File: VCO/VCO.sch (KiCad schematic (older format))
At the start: 22 parts, among them J1 JACK_STEREO, Q1 Q_NMOS_SGD, SW1 SWITCH_INV, U1 LM324

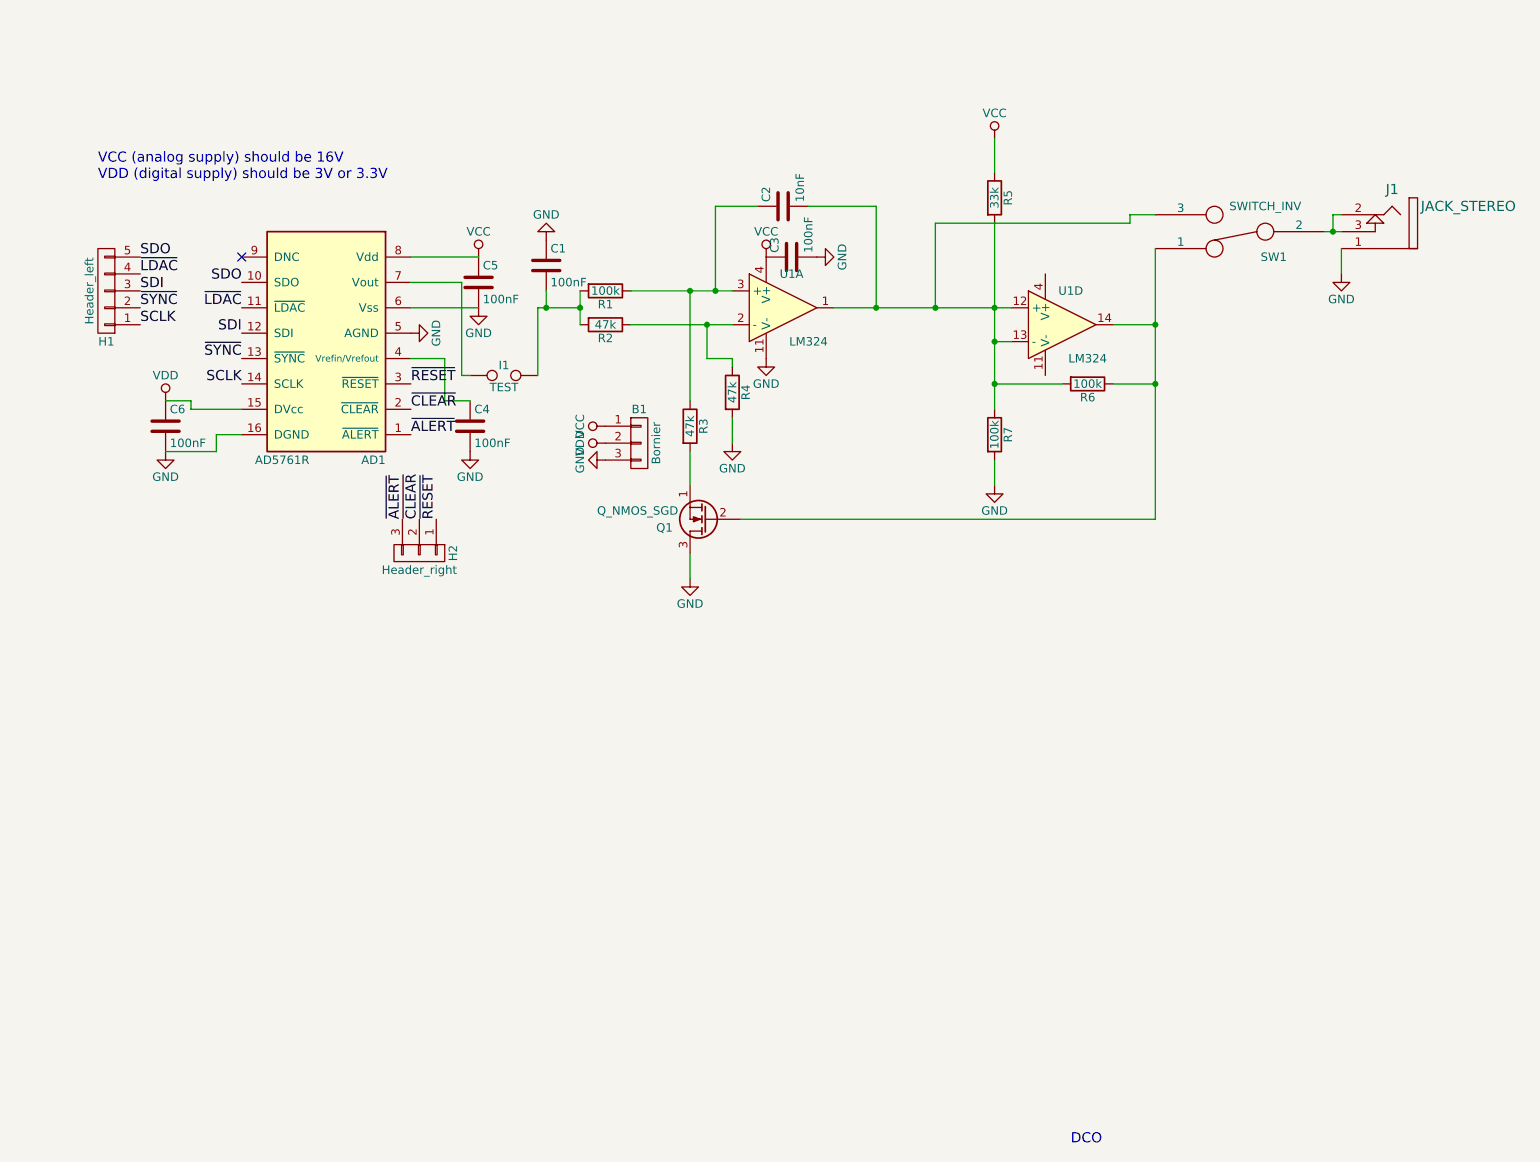
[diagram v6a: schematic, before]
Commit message: Fixed VCO
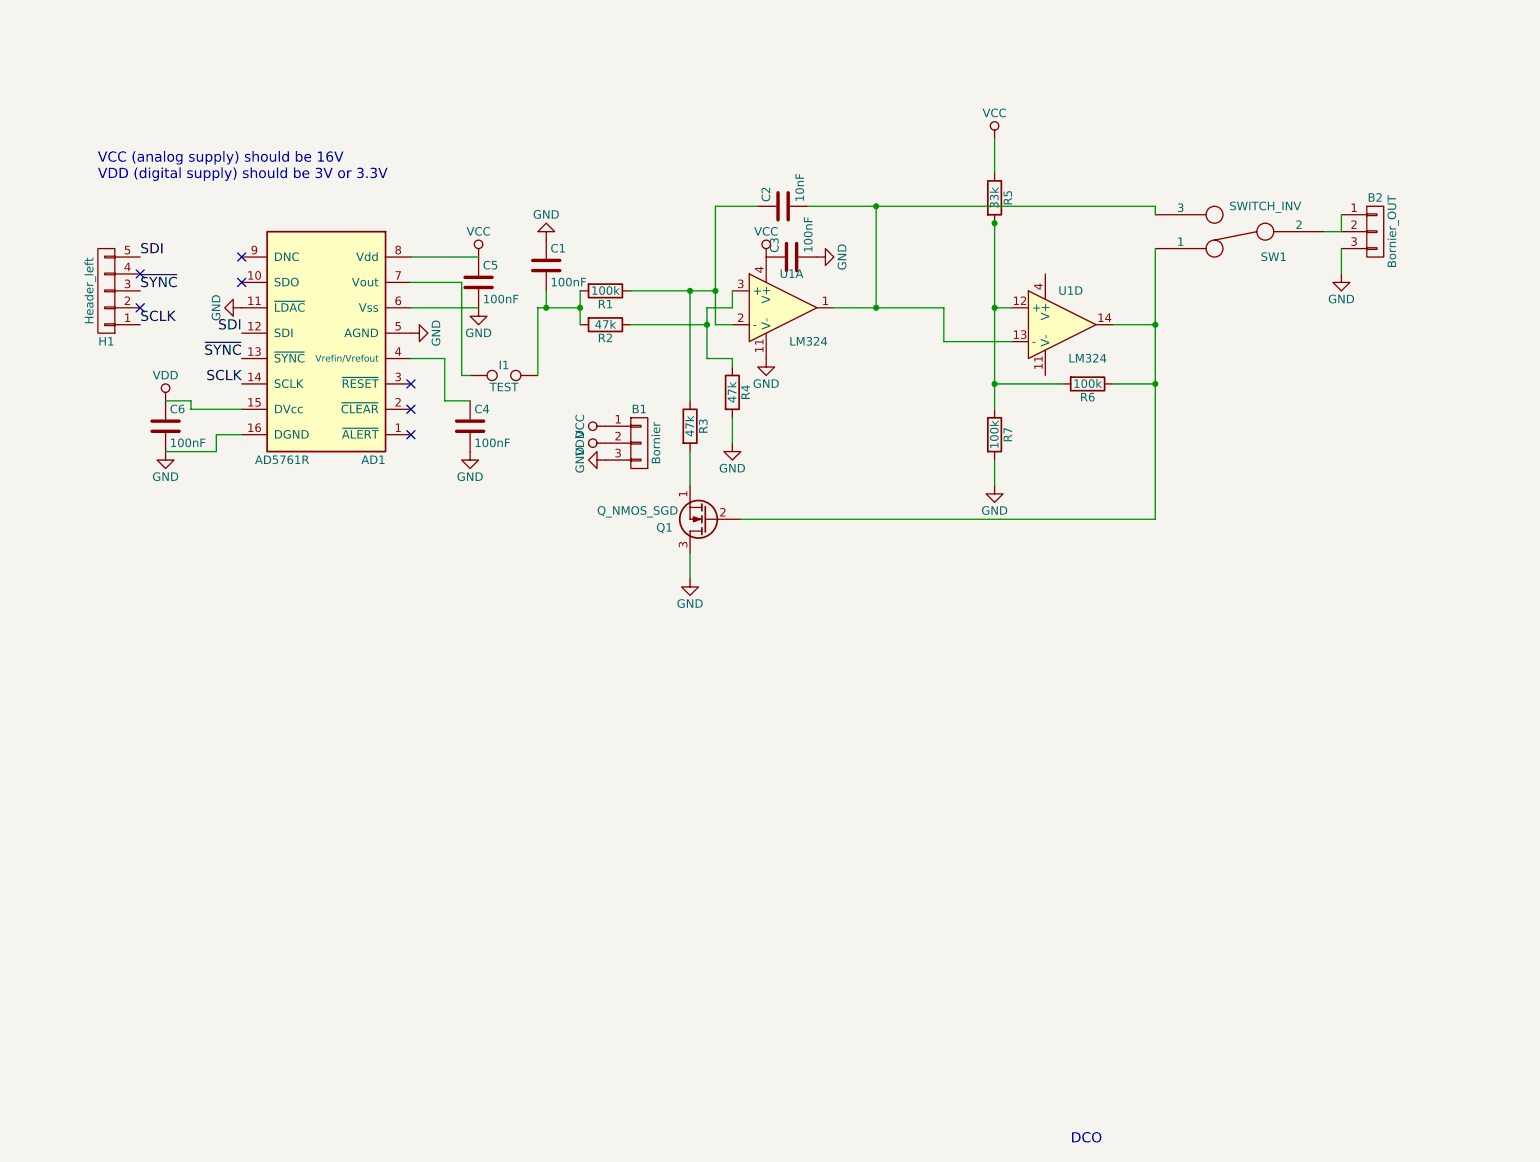
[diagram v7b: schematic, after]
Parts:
- removed H2: Header_right, Pin_Headers:Pin_Header_Straight_1x03_Pitch2.54mm, symbol CONN_01X03
- removed J1: JACK_STEREO, jack:jack-stereo, symbol JACK_MONO
- added B2: Bornier_OUT, bornier:Bornier_3pins, symbol CONN_01X03
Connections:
- net GND: now also AD1.11 (~LDAC), B2.3 (P3)
- net SDI: now also H1.5 (P5); no longer H1.3 (P3)
- net ~SYNC: now also H1.3 (P3); no longer H1.2 (P2)
- net at C2.1, R1.1, R3.1: now also U1.2 (-); no longer U1.3 (+)
- net at C2.2, SW1.3, U1.1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: no longer R5.2, R6.2, R7.1, U1.12 (+)
- net at R2.1, R4.1: now also U1.3 (+); no longer U1.2 (-)
- net at SW1.2: now also B2.1 (P1), B2.2 (P2)
- net SDO: no longer names the net of AD1.10 (SDO)
- net SDO: no longer H1.5 (P5)
- net ~ALERT: no longer names the net of AD1.1 (~ALERT)
- net ~CLEAR: no longer names the net of AD1.2 (~CLEAR)
- net ~LDAC: no longer names the net of H1.4 (P4)
- net ~LDAC: no longer AD1.11 (~LDAC)
- net ~RESET: no longer names the net of AD1.3 (~RESET)
- new net: R5.2, R6.2, R7.1, U1.12 (+)
- no-connect marks 1 -> 7
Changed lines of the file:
@@
-$EndComp
-$Comp
-L JACK_MONO J1
-U 1 1 58D1CA56
-P 9300 2100
-F 0 "J1" H 9300 2350 60  0000 C CNN
-F 1 "JACK_STEREO" H 9750 2250 60  0000 C CNN
-F 2 "jack:jack-stereo" H 9550 2150 60  0001 C CNN
-F 3 "" H 9550 2150 60  0000 C CNN
-	1    9300 2100
-	1    0    0    -1
 $EndComp
 $Comp
@@
 $EndComp
 NoConn ~ 2500 2250
-Text Label 2500 2400 2    60   ~ 0
-SDO
-Text Label 1900 2250 0    60   ~ 0
-SDO
-Text Label 2500 2550 2    60   ~ 0
-~LDAC
-Text Label 1900 2350 0    60   ~ 0
-~LDAC
 $Comp
 L C C6
@@
 Text Label 2500 2850 2    60   ~ 0
 ~SYNC
-Text Label 1900 2550 0    60   ~ 0
+Text Label 1900 2450 0    60   ~ 0
 ~SYNC
 Text Label 2500 3000 2    60   ~ 0
@@
 Text Label 1900 2650 0    60   ~ 0
 SCLK
-Text Label 3500 3000 0    60   ~ 0
-~RESET
-Text Label 3650 3800 1    60   ~ 0
-~RESET
-Text Label 3500 3150 0    60   ~ 0
-~CLEAR
-Text Label 3550 3800 1    60   ~ 0
-~CLEAR
-Text Label 3500 3300 0    60   ~ 0
-~ALERT
-Text Label 3450 3800 1    60   ~ 0
-~ALERT
 $Comp
 L C C5
@@
 Text Label 2500 2700 2    60   ~ 0
 SDI
-Text Label 1900 2450 0    60   ~ 0
+Text Label 1900 2250 0    60   ~ 0
 SDI
 $Comp
@@
 	-1   0    0    1
 $EndComp
-Wire Wire Line
-	4800 2650 5400 2650
-Wire Wire Line
-	4800 2450 5400 2450
-Wire Wire Line
-	5150 2450 5150 3100
-Connection ~ 5150 2450
-Wire Wire Line
-	5150 3400 5150 3600
-Wire Wire Line
-	5150 4000 5150 4150
-Wire Wire Line
-	5250 2650 5250 2850
-Wire Wire Line
-	5250 2850 5400 2850
-Wire Wire Line
-	5400 2850 5400 2900
-Connection ~ 5250 2650
-Wire Wire Line
-	5400 3200 5400 3350
-Wire Wire Line
-	5300 2450 5300 1950
-Wire Wire Line
-	5300 1950 5550 1950
-Connection ~ 5300 2450
-Connection ~ 6250 2550
-Wire Wire Line
-	6950 3000 7350 3000
-Wire Wire Line
-	6950 2050 6950 3150
-Connection ~ 6950 2550
-Wire Wire Line
-	6950 2750 7050 2750
-Connection ~ 6950 2750
-Wire Wire Line
-	6950 1550 6950 1750
-Connection ~ 6950 3000
-Wire Wire Line
-	6950 3450 6950 3600
-Wire Wire Line
-	7900 3800 5450 3800
-Wire Wire Line
-	7900 2200 7900 3800
-Wire Wire Line
-	7650 3000 7900 3000
-Connection ~ 7900 3000
-Connection ~ 4500 2550
-Wire Wire Line
-	4300 2450 4300 2550
-Connection ~ 4300 2550
-Wire Wire Line
-	6600 2050 6600 2550
-Connection ~ 6600 2550
-Connection ~ 7900 2650
-Wire Wire Line
-	6250 1950 6250 2550
-Wire Wire Line
-	6000 2550 7050 2550
-Wire Wire Line
-	4500 2550 4250 2550
-Wire Wire Line
-	4250 2550 4250 2950
-Wire Wire Line
-	3500 2400 3800 2400
-Wire Wire Line
-	3800 2400 3800 2950
-Wire Wire Line
-	3800 2950 3850 2950
-Wire Wire Line
-	3500 2850 3700 2850
-Wire Wire Line
-	3700 2850 3700 3100
-Wire Wire Line
-	4500 2450 4500 2650
-Wire Wire Line
-	3500 2250 3900 2250
-Wire Wire Line
-	3700 3100 3850 3100
-Wire Wire Line
-	6250 1950 5850 1950
-Wire Wire Line
-	2500 3300 2350 3300
-Wire Wire Line
-	2350 3300 2350 3400
-Wire Wire Line
-	2350 3400 2050 3400
-Wire Wire Line
-	2500 3150 2200 3150
-Wire Wire Line
-	2200 3150 2200 3100
-Wire Wire Line
-	3500 2550 3900 2550
-Wire Wire Line
-	2200 3100 2050 3100
-Wire Wire Line
-	7650 2650 7900 2650
-Wire Wire Line
-	6600 2050 7750 2050
-Wire Wire Line
-	7750 2050 7750 2000
-Wire Wire Line
-	7750 2000 7900 2000
-Wire Wire Line
-	8900 2100 9000 2100
-Wire Wire Line
-	8950 2100 8950 2000
-Wire Wire Line
-	8950 2000 9000 2000
-Connection ~ 8950 2100
-Wire Wire Line
-	9000 2350 9000 2200
 $Comp
 L CONN_01X05 H1
@@
 	-1   0    0    1
 $EndComp
-$Comp
-L CONN_01X03 H2
-U 1 1 58EFE144
-P 3550 4000
-F 0 "H2" H 3550 4200 50  0000 C CNN
-F 1 "Header_right" V 3650 4000 50  0000 C CNN
-F 2 "Pin_Headers:Pin_Header_Straight_1x03_Pitch2.54mm" H 3550 4000 50  0001 C CNN
-F 3 "" H 3550 4000 50  0000 C CNN
-	1    3550 4000
+Wire Wire Line
+	5150 3400 5150 3600
+Wire Wire Line
+	5150 4000 5150 4150
+Wire Wire Line
+	5250 2550 5250 2850
+Wire Wire Line
+	5250 2850 5400 2850
+Wire Wire Line
+	5400 2850 5400 2900
+Connection ~ 5250 2650
+Wire Wire Line
+	5400 3200 5400 3350
+Wire Wire Line
+	5300 1950 5300 2650
+Wire Wire Line
+	5300 1950 5550 1950
+Connection ~ 5300 2450
+Connection ~ 6250 2550
+Wire Wire Line
+	6650 2750 7050 2750
+Wire Wire Line
+	6950 1550 6950 1750
+Wire Wire Line
+	6950 3450 6950 3600
+Wire Wire Line
+	7900 3800 5450 3800
+Wire Wire Line
+	7900 2200 7900 3800
+Wire Wire Line
+	7650 3000 7900 3000
+Connection ~ 7900 3000
+Connection ~ 4500 2550
+Wire Wire Line
+	4300 2450 4300 2550
+Connection ~ 4300 2550
+Connection ~ 7900 2650
+Wire Wire Line
+	6250 1950 6250 2550
+Wire Wire Line
+	4500 2550 4250 2550
+Wire Wire Line
+	4250 2550 4250 2950
+Wire Wire Line
+	3500 2400 3800 2400
+Wire Wire Line
+	3800 2400 3800 2950
+Wire Wire Line
+	3800 2950 3850 2950
+Wire Wire Line
+	3500 2850 3700 2850
+Wire Wire Line
+	3700 2850 3700 3100
+Wire Wire Line
+	4500 2450 4500 2650
+Wire Wire Line
+	3500 2250 3900 2250
+Wire Wire Line
+	3700 3100 3850 3100
+Wire Wire Line
+	5850 1950 7900 1950
+Wire Wire Line
+	2500 3300 2350 3300
+Wire Wire Line
+	2350 3300 2350 3400
+Wire Wire Line
+	2350 3400 2050 3400
+Wire Wire Line
+	2500 3150 2200 3150
+Wire Wire Line
+	2200 3150 2200 3100
+Wire Wire Line
+	3500 2550 3900 2550
+Wire Wire Line
+	2200 3100 2050 3100
+Wire Wire Line
+	7650 2650 7900 2650
+Wire Wire Line
+	8900 2100 9000 2100
+Wire Wire Line
+	9000 2350 9000 2200
+Wire Wire Line
+	5400 2450 5400 2550
+Wire Wire Line
+	5400 2550 5250 2550
+Wire Wire Line
+	5300 2650 5400 2650
+Wire Wire Line
+	4800 2450 5300 2450
+Wire Wire Line
+	4800 2650 5250 2650
+Connection ~ 5150 2450
+Wire Wire Line
+	5150 2450 5150 3100
+Wire Wire Line
+	6950 2050 6950 3150
+Connection ~ 6950 2050
+Wire Wire Line
+	6000 2550 6650 2550
+Wire Wire Line
+	7900 1950 7900 2000
+Connection ~ 6250 1950
+Wire Wire Line
+	6650 2550 6650 2750
+Wire Wire Line
+	7050 2550 6950 2550
+Connection ~ 6950 2550
+Wire Wire Line
+	6950 3000 7350 3000
+Connection ~ 6950 3000
+$Comp
+L CONN_01X03 B2
+U 1 1 59021566
+P 9200 2100
+F 0 "B2" H 9200 2300 50  0000 C CNN
+F 1 "Bornier_OUT" V 9300 2100 50  0000 C CNN
+F 2 "bornier:Bornier_3pins" H 9200 2100 50  0001 C CNN
+F 3 "" H 9200 2100 50  0000 C CNN
+	1    9200 2100
+	1    0    0    -1
+$EndComp
+Wire Wire Line
+	9000 2100 9000 2000
+$Comp
+L GND #PWR019
+U 1 1 59021A14
+P 2500 2550
+F 0 "#PWR019" H 2500 2300 50  0001 C CNN
+F 1 "GND" H 2500 2400 50  0000 C CNN
+F 2 "" H 2500 2550 50  0000 C CNN
+F 3 "" H 2500 2550 50  0000 C CNN
+	1    2500 2550
 	0    1    1    0
 $EndComp
+NoConn ~ 1900 2350
+NoConn ~ 3500 3000
+NoConn ~ 3500 3150
+NoConn ~ 3500 3300
+NoConn ~ 2500 2400
+NoConn ~ 1900 2550
 $EndSCHEMATC
